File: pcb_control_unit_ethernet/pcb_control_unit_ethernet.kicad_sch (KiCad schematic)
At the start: 42 parts, among them J1 STDC14, J2 Micro_SD_Card_Det1, SW1 Reset, SW2 Boot, U1 STM32H563VITx, U10 SIT3051TK

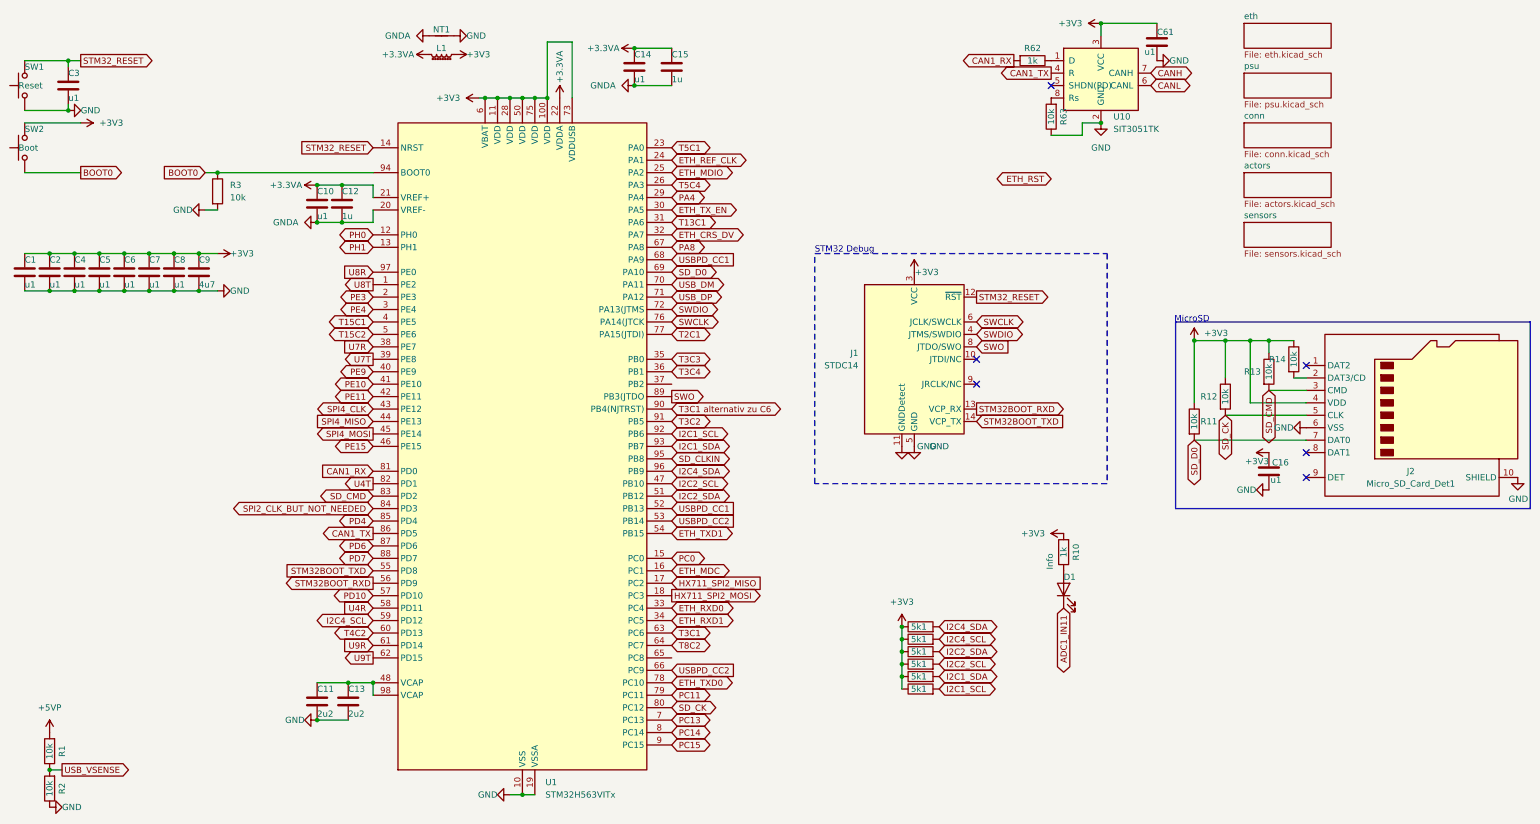
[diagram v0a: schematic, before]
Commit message: First time zero errors, but bad layout
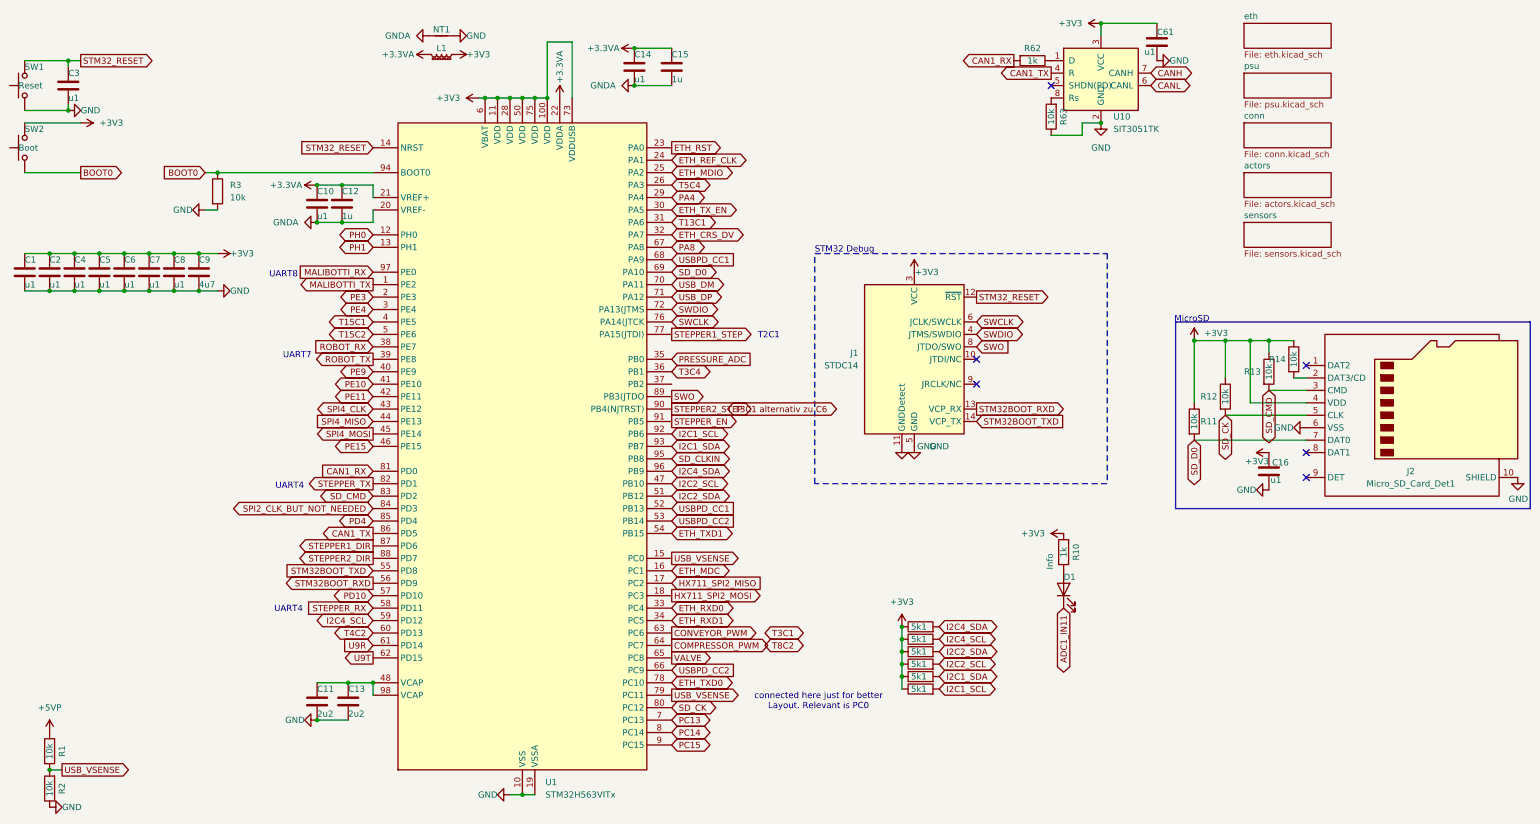
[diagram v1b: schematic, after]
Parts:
- R63: footprint Resistor_SMD:R_0402_1005Metric -> Resistor_SMD:R_0201_0603Metric
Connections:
- net PC0 is gone; now on net USB_VSENSE: U1.15 (PC0)
- net PC11 is gone; now on net USB_VSENSE: U1.79 (PC11)
- net T5C1 is gone; now on net ETH_RST: U1.23 (PA0)
- net T3C1: no longer U1.63 (PC6)
- net T3C1 alternativ zu C6: no longer U1.90 (PB4(NJTRST))
- net T8C2: no longer U1.64 (PC7)
- net VALVE: now reaches U1.65 (PC8)
- net PD6 renamed STEPPER1_DIR
- net PD7 renamed STEPPER2_DIR
- net T2C1 renamed STEPPER1_STEP
- net T3C2 renamed STEPPER_EN
- net T3C3 renamed PRESSURE_ADC
- net U4R renamed STEPPER_RX
- net U4T renamed STEPPER_TX
- net U7R renamed ROBOT_RX
- net U7T renamed ROBOT_TX
- net U8R renamed MALIBOTTI_RX
- net U8T renamed MALIBOTTI_TX
- new net COMPRESSOR_PWM: U1.64 (PC7)
- new net CONVEYOR_PWM: U1.63 (PC6)
- new net STEPPER2_STEP: U1.90 (PB4(NJTRST))
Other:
- note added: "T2C1"
- note added: "UART4"
- note added: "UART7"
- note added: "UART8"
- note added: "connected here just for better Layout. Relevant is PC0"

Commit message: WIP
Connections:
- net PE15 is gone; now on net LED_INFO: U1.46 (PE15)
- net ADC1_IN11 renamed LED_INFO
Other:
- added sheet EtherCAT (ethercat_esc.kicad_sch)
- note added: "TIMER-Nutzung: T8 -->Conveyor + Compressor T3 --> Stepper2 T2 --> Stepper1 UART-Nutzung U4 -->Stepper U7 --> 6DOF-Robot U8 --> Malibotti"
